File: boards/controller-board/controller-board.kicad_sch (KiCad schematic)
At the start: 71 parts, among them J1 Conn_01x02, J2 Conn_01x02, J3 Conn_01x02, J4 Conn_01x02, J5 Conn_01x03, J6 Phoenix 1995499, Q1 PMV45EN, Q2 Goford_G11S_20V_11A, SW1 EG1271, U1 LTC3624, U2 ADS1015IRUGR, U3 ADS1015IRUGR, U4 RPi_Pico, U5 MCP4728

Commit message: minor changes
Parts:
- C1, C15: DPN 1276-CL32B226MOJVPNECT-ND -> 1276-3392-1-ND; MPN CL32B226MOJVPNE -> CL32B226KAJNNNE
- C16: DPN 311-1446-1-ND -> 1276-1102-1-ND; MFR Yageo -> Samsung Electro-Mechanics; MPN CC0603KRX7R7BB105 -> CL10A105KA8NNNC
- C2: DPN 490-6328-1-ND -> 1276-1006-1-ND; MFR Murata Electronics -> Samsung Electro-Mechanics; MPN GRM155R71C104KA88J -> CL10B104KA8NNNC
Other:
- note removed: "should C15 and C1 have higher voltage ratings?"
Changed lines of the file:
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@@
 		)
 	)
-	(text "should C15 and C1 have higher voltage ratings?"
-		(exclude_from_sim no)
-		(at 323.088 27.94 0)
-		(effects
-			(font
-				(size 2.54 2.54)
-				(thickness 0.508)
-				(bold yes)
-				(color 255 57 88 1)
-			)
-		)
-	)
 	(text "Halogen Dimming"
 		(exclude_from_sim no)
@@
 	)
 	(label "BLUE_LIM"
-		(at 401.32 314.96 0)
+		(at 400.05 314.96 0)
 		(fields_autoplaced yes)
 		(effects
@@
 			)
 		)
-		(property "DPN" "311-1446-1-ND"
+		(property "DPN" "1276-1102-1-ND"
 			(at 379.73 52.07 0)
 			(effects
@@
 			)
 		)
-		(property "MFR" "Yageo"
+		(property "MFR" "Samsung Electro-Mechanics"
 			(at 379.73 52.07 0)
 			(effects
@@
 			)
 		)
-		(property "MPN" "CC0603KRX7R7BB105 "
+		(property "MPN" "CL10A105KA8NNNC"
 			(at 379.73 52.07 0)
 			(effects
@@
 			)
 		)
-		(property "DPN" "1276-CL32B226MOJVPNECT-ND"
+		(property "DPN" "1276-3392-1-ND"
 			(at 372.11 52.07 0)
 			(effects
@@
 			)
 		)
-		(property "MPN" "CL32B226MOJVPNE"
+		(property "MPN" "CL32B226KAJNNNE"
 			(at 372.11 52.07 0)
 			(effects
@@
 			)
 		)
-		(property "DPN" "490-6328-1-ND"
+		(property "DPN" "1276-1006-1-ND"
 			(at 199.39 71.12 0)
 			(effects
@@
 			)
 		)
-		(property "MPN" "GRM155R71C104KA88J"
+		(property "MPN" "CL10B104KA8NNNC"
 			(at 199.39 71.12 0)
 			(effects
@@
 			)
 		)
-		(property "MFR" "Murata Electronics"
+		(property "MFR" "Samsung Electro-Mechanics"
 			(at 199.39 71.12 0)
 			(effects
@@
 			)
 		)
-		(property "DPN" "1276-CL32B226MOJVPNECT-ND"
+		(property "DPN" "1276-3392-1-ND"
 			(at 191.77 71.12 0)
 			(effects
@@
 			)
 		)
-		(property "MPN" "CL32B226MOJVPNE"
+		(property "MPN" "CL32B226KAJNNNE"
 			(at 191.77 71.12 0)
 			(effects

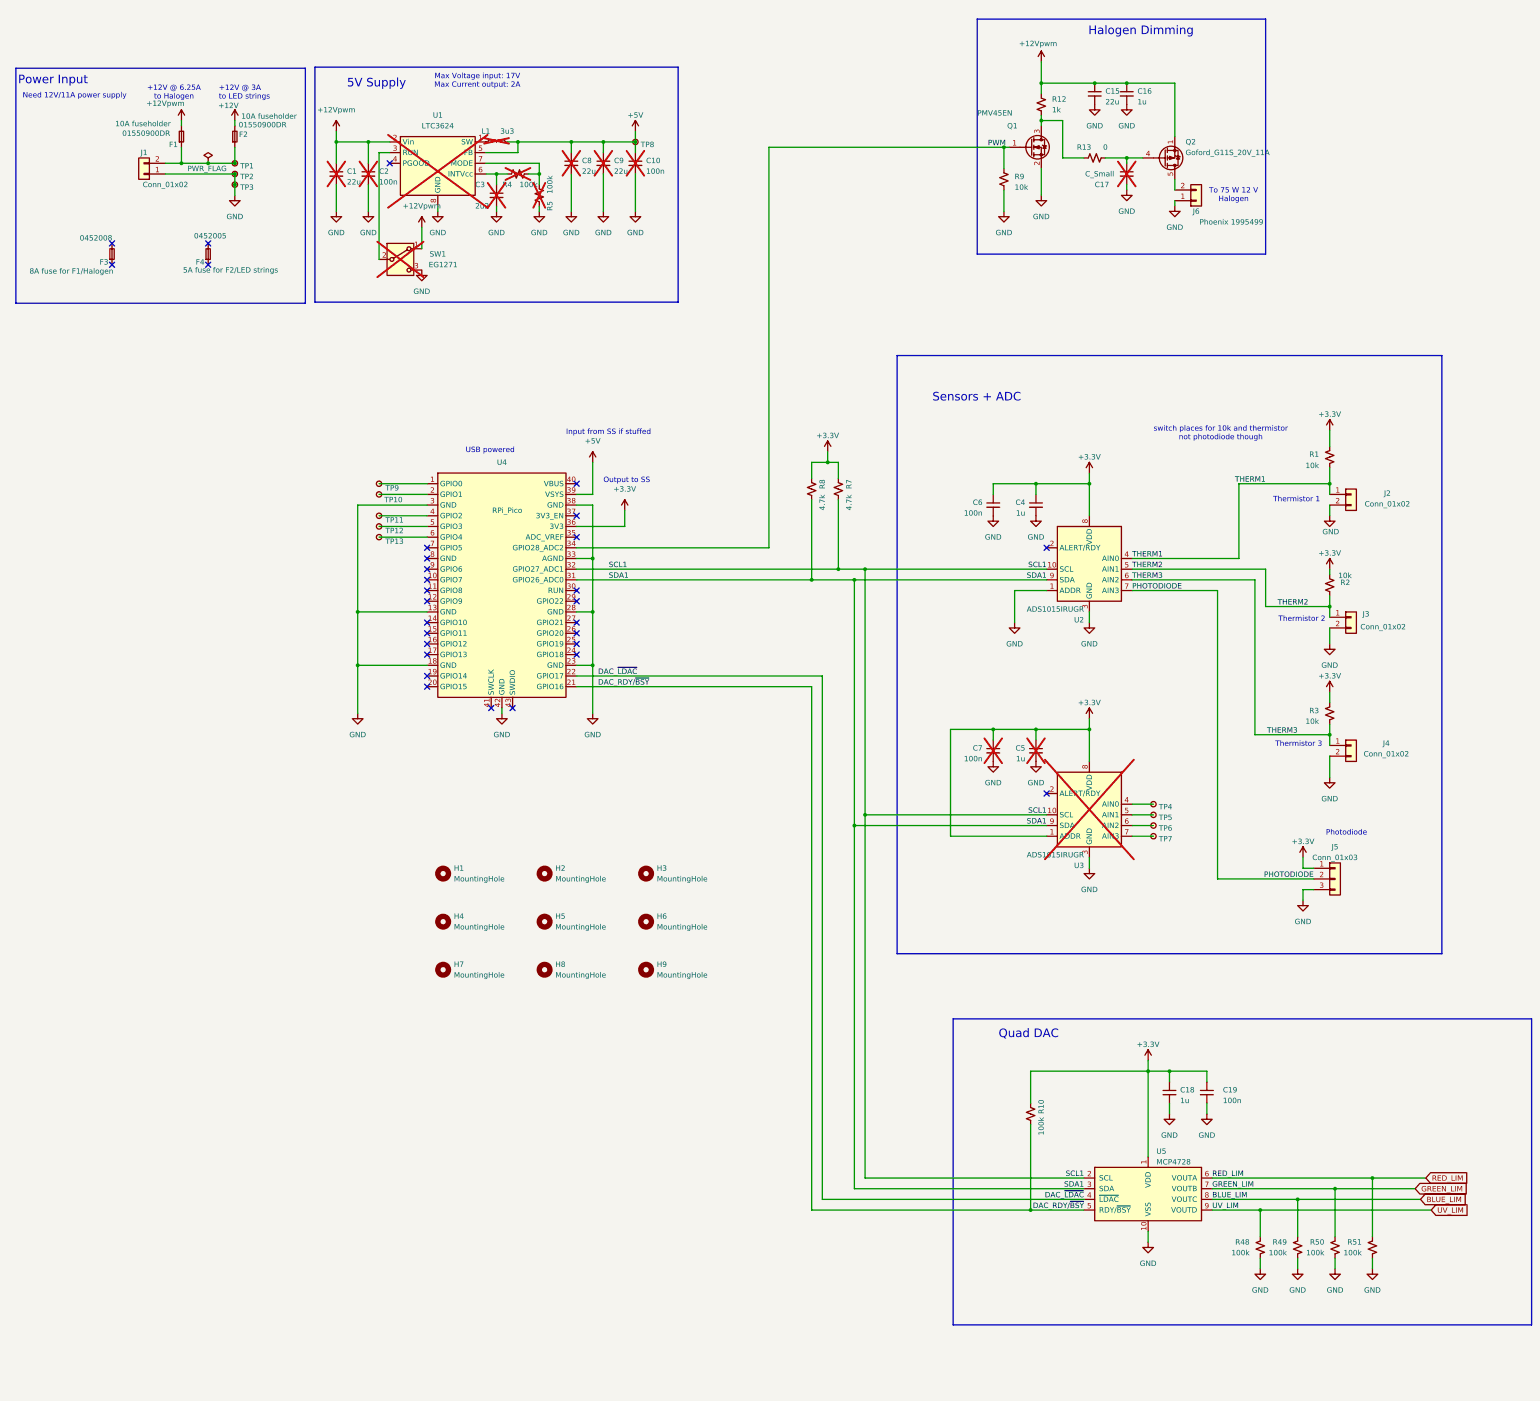
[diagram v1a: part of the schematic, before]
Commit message: Andrew polishing: arbitrary schematic changes to make it pretty, and then updating zones to have fillets and smaller widths, and a billion ground vias.
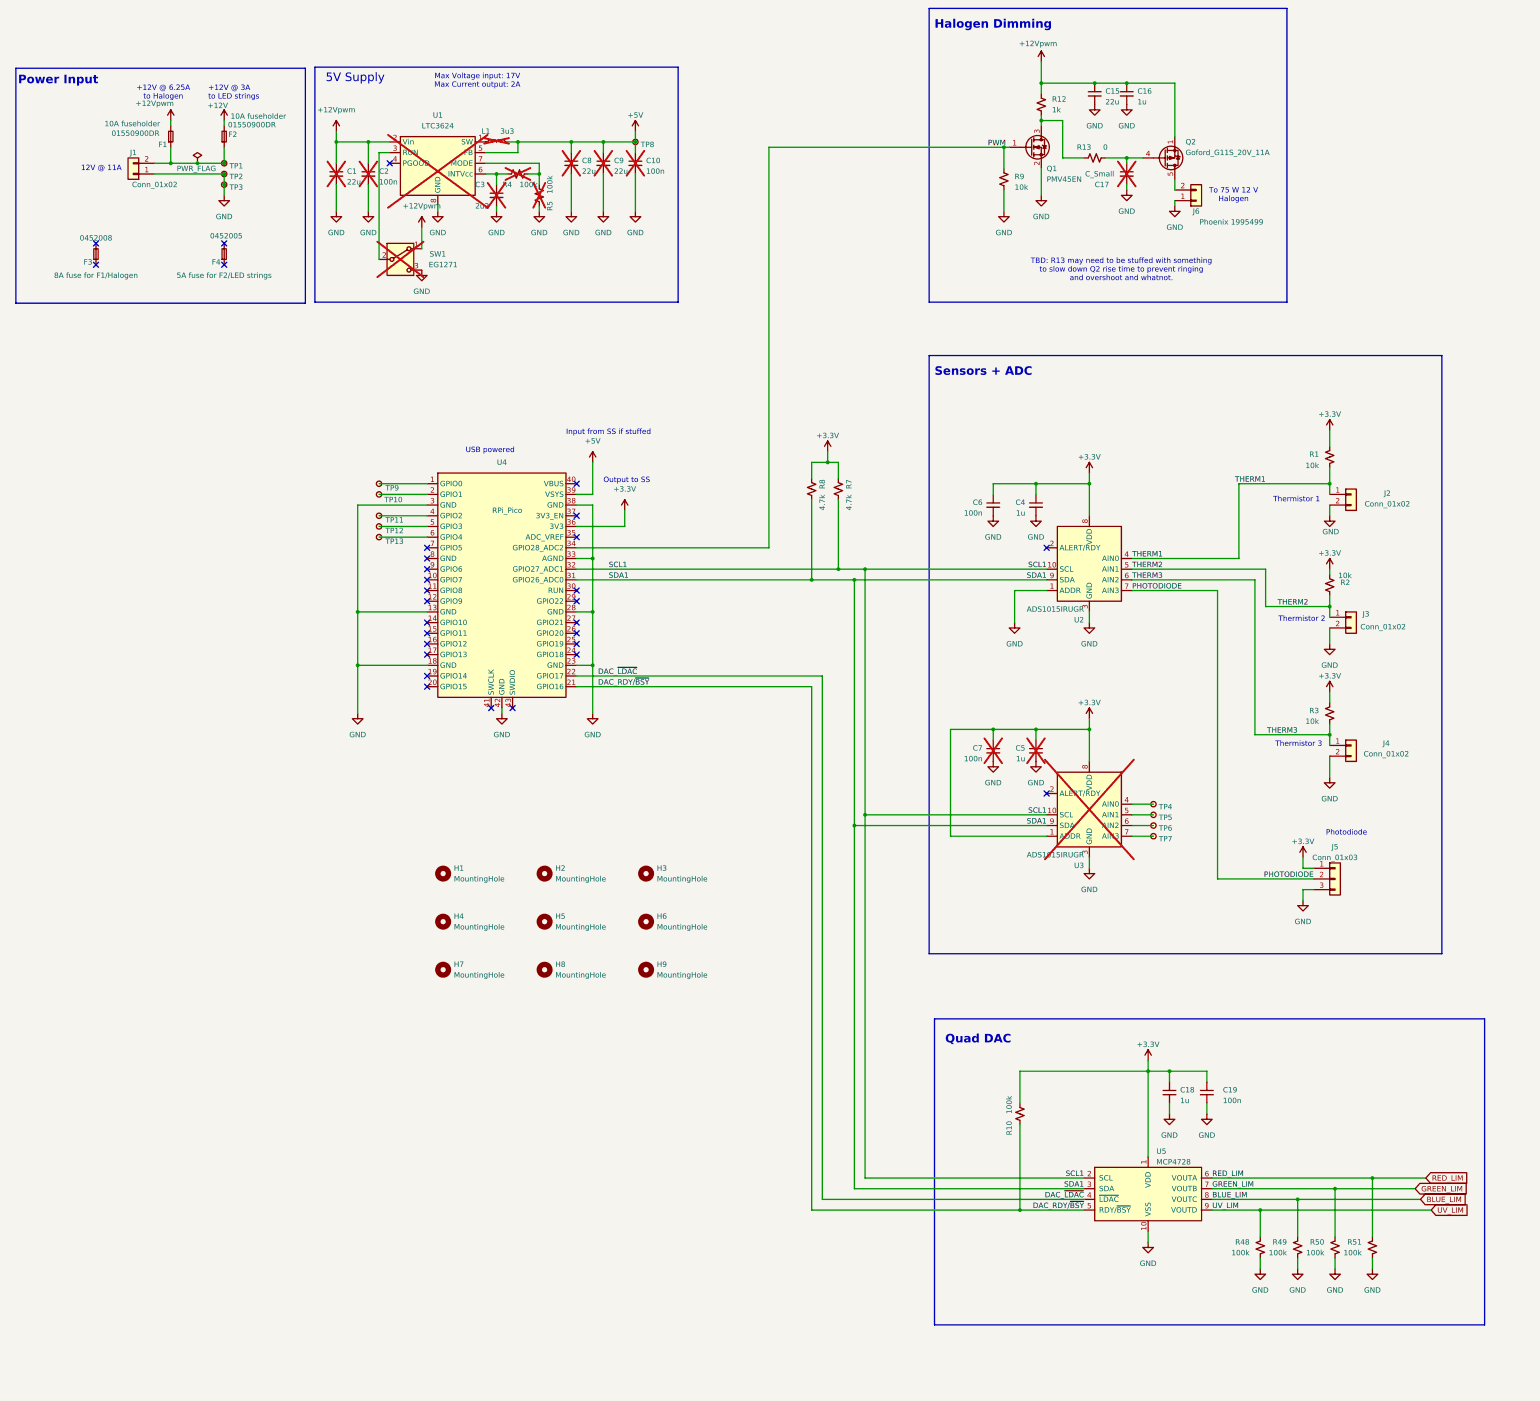
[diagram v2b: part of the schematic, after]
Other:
- note added: "12V @ 11A"
- note added: "TBD: R13 may need to be stuffed with something to slow down Q2 rise time to prevent ringing and overshoot and whatnot."
- note removed: "Need 12V/11A power supply"
- note removed: "switch places for 10k and thermistor not photodiode though"
- moved on the sheet: F1, F2, F3, F4, J1, R10, TP1, TP2, TP3
